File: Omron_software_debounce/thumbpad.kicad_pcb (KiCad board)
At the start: 2 copper layers, 36 x 30 mm, 19 parts, among them J1 Conn_01x06, SW1 D2LS-2120M, SW2 D2LS-2120M, SW3 D2LS-2120M, SW4 D2LS-2120M

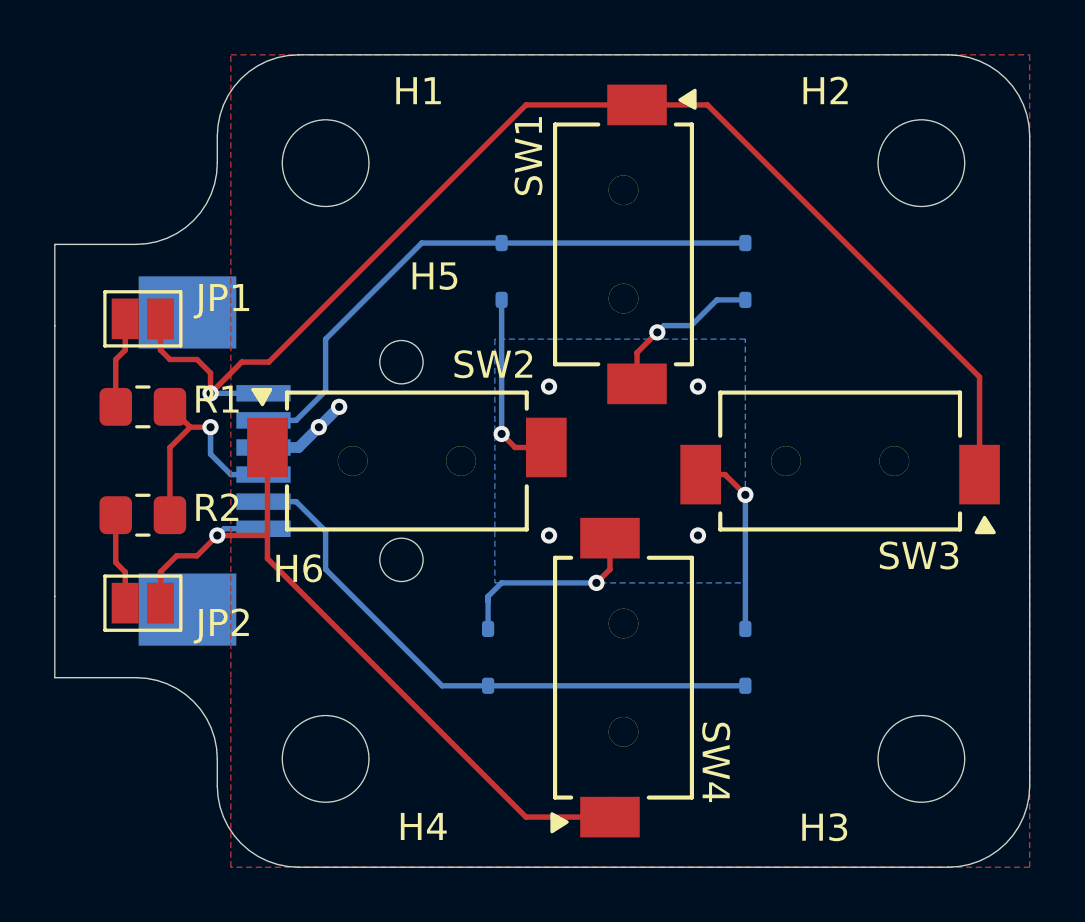
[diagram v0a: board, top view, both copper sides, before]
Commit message: Added pth pads for hand solder/pin headers
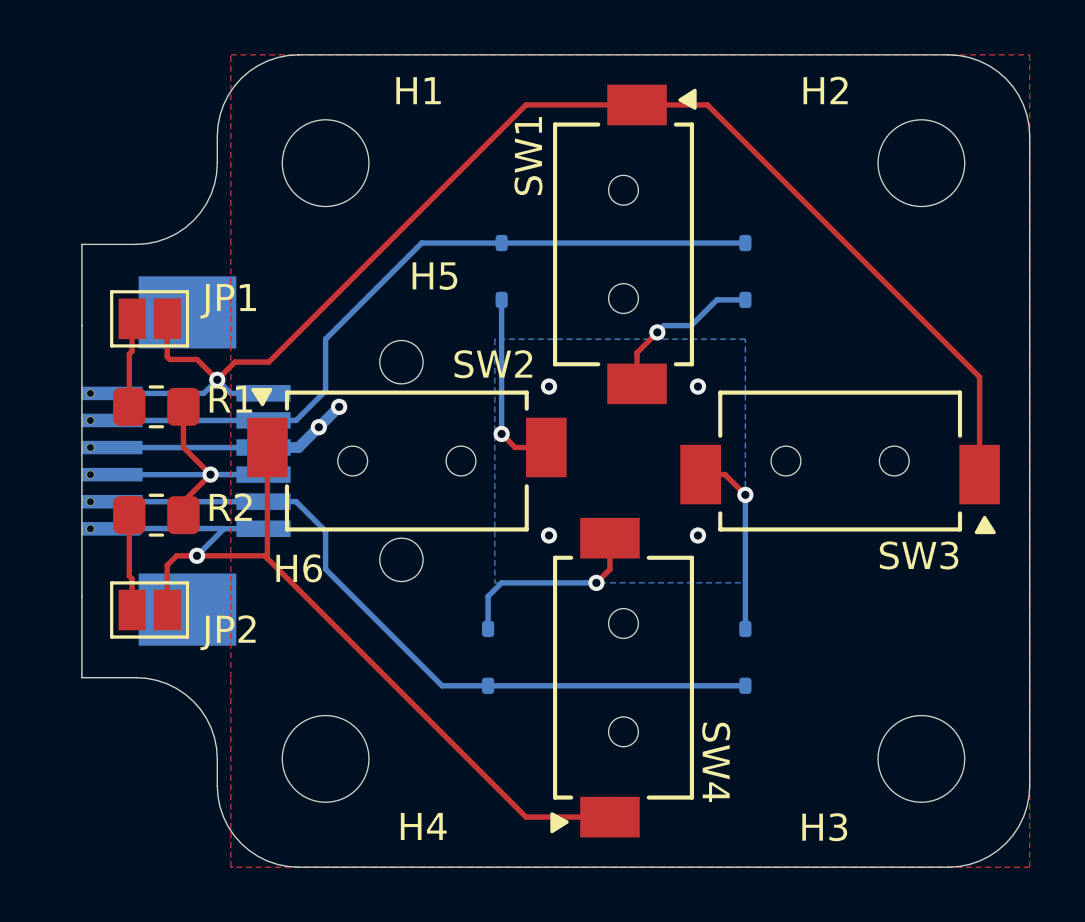
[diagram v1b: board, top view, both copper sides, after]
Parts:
- added J2: Conn_01x06, My_Library:pads_connector_0.1mm, B.Cu at (131.1, 80.0)
- moved R1 0.50 mm to (132.8, 78.0)
- moved R2 0.50 mm to (132.8, 82.0)
- moved JP2 0.35 mm to (132.5, 85.5)
- moved JP1 0.25 mm to (132.5, 74.8)
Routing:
- net GND: track 3.42 -> 9.01 mm
- net Row2: track 21.4 -> 27.0 mm
- net Row1: track 21.6 -> 27.2 mm
- net Col2: track 29.0 -> 33.9 mm
- net Col1: track 46.6 -> 49.7 mm
- net +5V: track 8.64 -> 10.4 mm
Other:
- board size 36 x 30 mm -> 35 x 30 mm
